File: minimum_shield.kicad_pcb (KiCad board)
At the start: 2 copper layers, 14 parts, among them J1 Conn_02x08_Odd_Even, J2 Conn_02x08_Odd_Even, J3 Conn_01x06, SW1 SW_Push

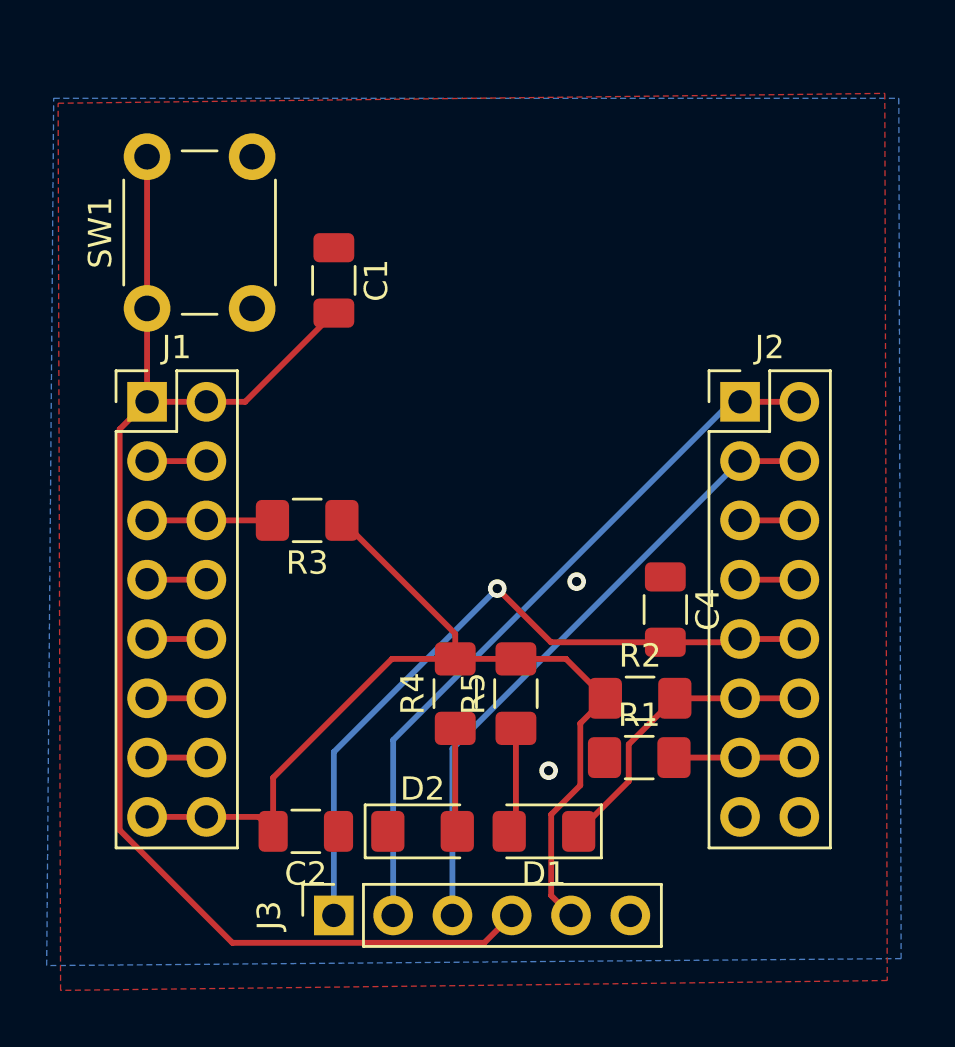
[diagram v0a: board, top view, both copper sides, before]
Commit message: V1.1 - fixing missing ground connection to pull up resistor for GPIO15
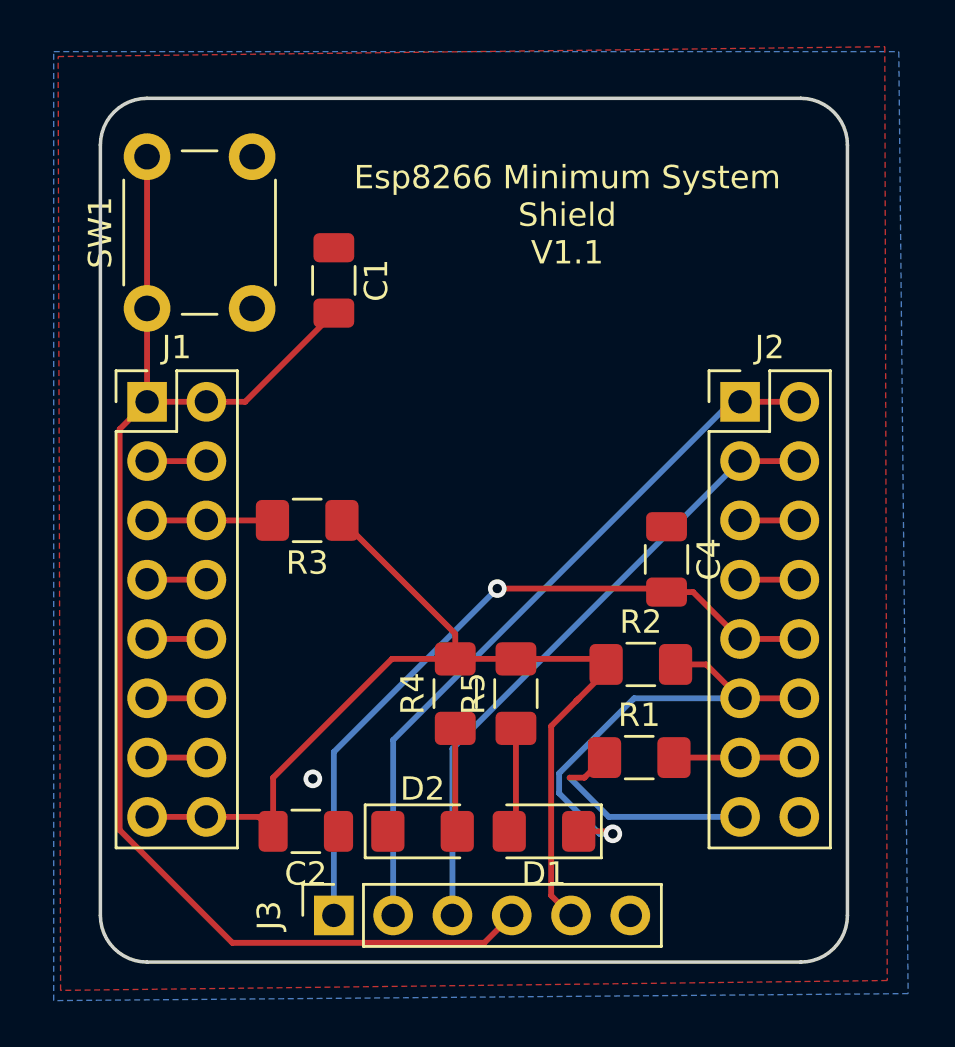
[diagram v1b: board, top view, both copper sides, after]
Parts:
- moved C4 2.15 mm to (22.2, 6.75)
- moved R2 1.45 mm to (21.1, 11.2)
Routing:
- net GND: track 0.00 -> 9.85 mm, vias 2 -> 1
- net IO2: track 12.7 -> 20.4 mm, vias 0 -> 1
- net VCC: track 44.0 -> 45.0 mm
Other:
- board outline added: 32 x 37 mm
- board text added: "Esp8266 Minimum System Shield V1.1"
- board text removed: "GPIO2"
